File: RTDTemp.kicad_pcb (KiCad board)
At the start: 2 copper layers, 80 x 100 mm, 109 parts, among them J1 Conn_01x02, J2 Conn_01x02, J3 Car Power, J4 CAN_In, J5 CAN_Out, SW1 SW_Push, U1 Nucleo_L432KC, U2 PWR_REG_PQMC3-Dx-Sx-S, U3 ADM3055E, U4 CDSOT23-T24CAN

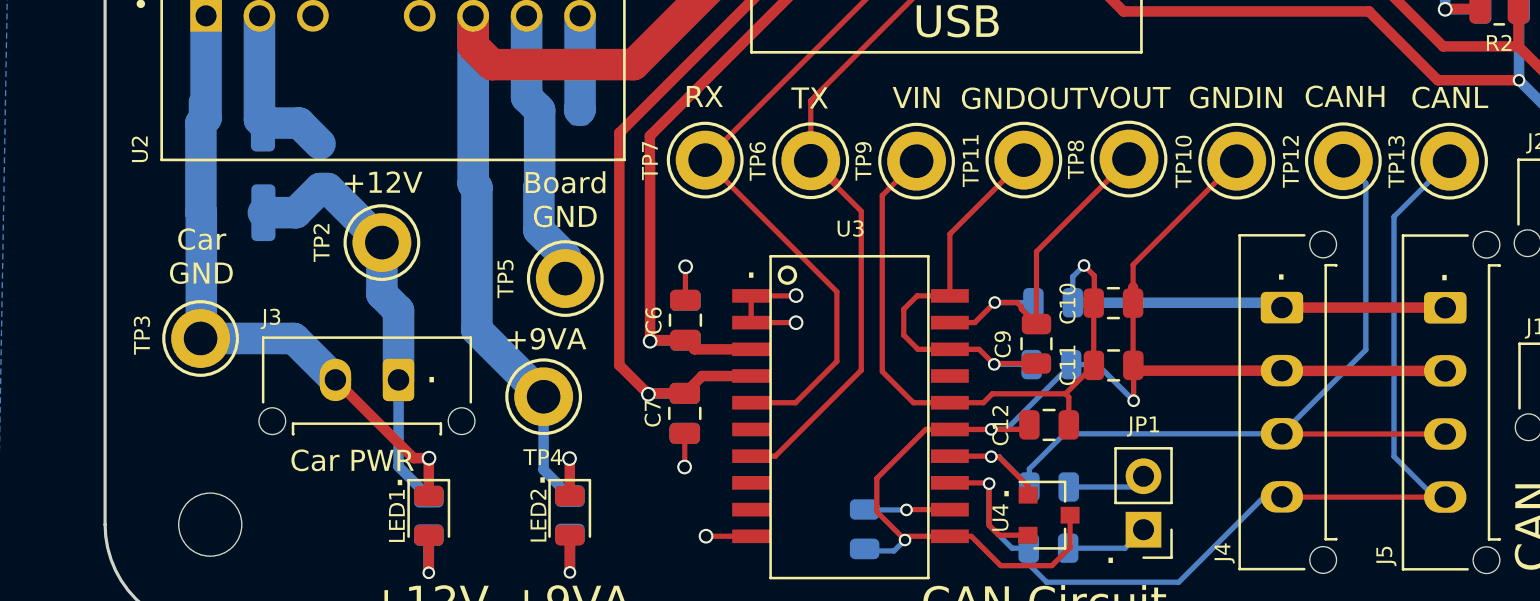
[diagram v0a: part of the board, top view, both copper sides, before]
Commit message: Updated README with assembly and testing instructions.
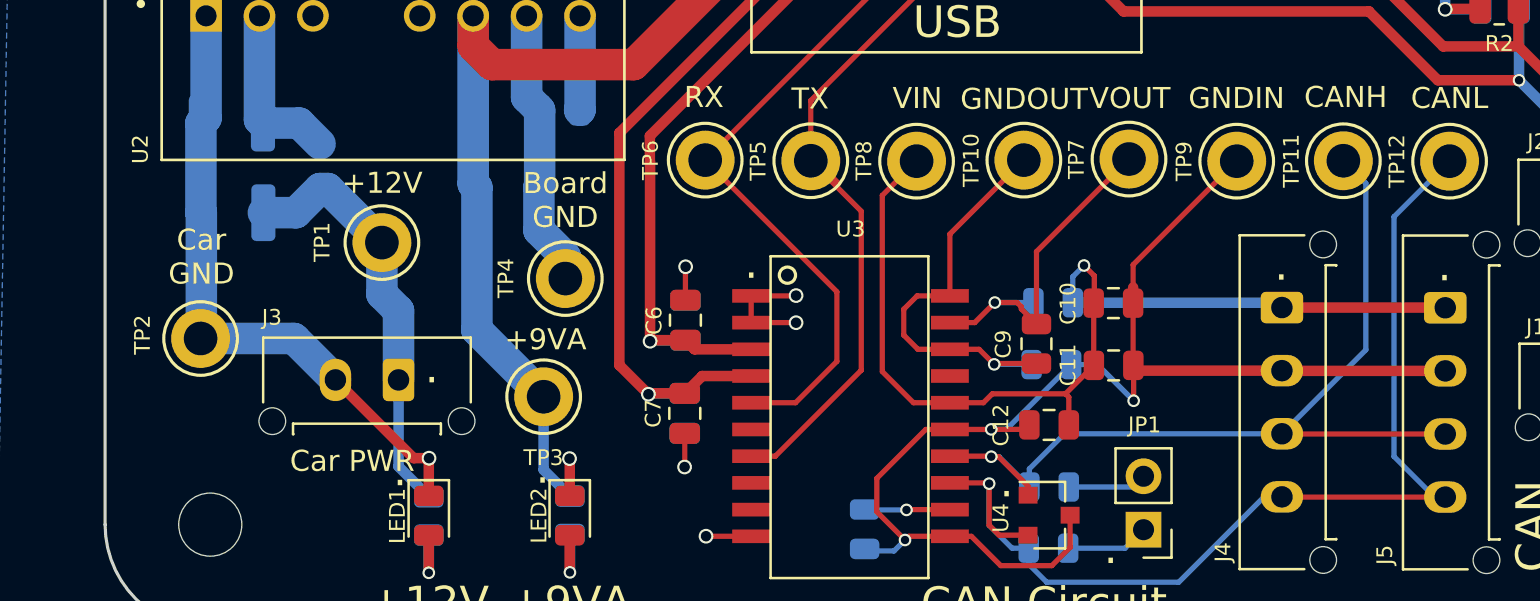
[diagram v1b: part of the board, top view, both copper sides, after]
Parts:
- renumbered TP2 to TP1, TP11 to TP10, TP12 to TP11, TP13 to TP12, TP3 to TP2, TP4 to TP3, TP5 to TP4, TP6 to TP5, TP7 to TP6, TP8 to TP7, TP9 to TP8, TP10 to TP9
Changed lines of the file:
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@@
   (general
     (thickness 1.6)
-    (drawings 224)
+    (drawings 223)
     (tracks 1386)
     (zones 0)
@@
   (page USLetter)
   (title_block
-    (title "UT SVT MPPT 2018")
-    (date 2018-10-31)
-    (rev Rev1.2+)
+    (title "Array RTD/Irradiance Sensor Board")
+    (date 2020-12-13)
+    (rev 1.0.0)
     (company "UT Solar Vehicle Team")
-    (comment 1 "See Schematic Rev3.1+.")
+    (comment 1 "Matthew Yu")
+    (comment 2 "Jacob Giddens")
+    (comment 3 "Gary Hallock")
   )
   (layers
@@
     (38 B.Mask user)
     (39 F.Mask user)
-    (40 Dwgs.User user hide)
-    (41 Cmts.User user hide)
+    (40 Dwgs.User user)
+    (41 Cmts.User user)
     (42 Eco1.User user)
     (43 Eco2.User user)
@@
     (descr "Keystone Miniature THM Test Point 5005-5009, http://www.keyelco.com/product-pdf.cfm?p=1314")
     (tags "Through Hole Mount Test Points")
-    (fp_text reference TP12 (at 0 -2.47 90) (layer F.SilkS)
+    (fp_text reference TP11 (at 0 -2.47 90) (layer F.SilkS)
       (effects (font (size 0.75 0.75) (thickness 0.15)))
     )
@@
     (descr "Keystone Miniature THM Test Point 5005-5009, http://www.keyelco.com/product-pdf.cfm?p=1314")
     (tags "Through Hole Mount Test Points")
-    (fp_text reference TP5 (at -2.82 -0.02 90) (layer F.SilkS)
+    (fp_text reference TP4 (at -2.82 -0.02 90) (layer F.SilkS)
       (effects (font (size 0.75 0.75) (thickness 0.15)))
     )
@@
     (descr "Keystone Miniature THM Test Point 5005-5009, http://www.keyelco.com/product-pdf.cfm?p=1314")
     (tags "Through Hole Mount Test Points")
-    (fp_text reference TP4 (at -0.01 2.9) (layer F.SilkS)
+    (fp_text reference TP3 (at -0.01 2.9) (layer F.SilkS)
       (effects (font (size 0.75 0.75) (thickness 0.15)))
     )
@@
     (descr "Keystone Miniature THM Test Point 5005-5009, http://www.keyelco.com/product-pdf.cfm?p=1314")
     (tags "Through Hole Mount Test Points")
-    (fp_text reference TP3 (at -2.76 -0.18 90) (layer F.SilkS)
+    (fp_text reference TP2 (at -2.76 -0.18 90) (layer F.SilkS)
       (effects (font (size 0.75 0.75) (thickness 0.15)))
     )
@@
     (descr "Keystone Miniature THM Test Point 5005-5009, http://www.keyelco.com/product-pdf.cfm?p=1314")
     (tags "Through Hole Mount Test Points")
-    (fp_text reference TP2 (at -2.84 -0.03 90) (layer F.SilkS)
+    (fp_text reference TP1 (at -2.84 -0.03 90) (layer F.SilkS)
       (effects (font (size 0.75 0.75) (thickness 0.15)))
     )
@@
     (descr "Keystone Miniature THM Test Point 5005-5009, http://www.keyelco.com/product-pdf.cfm?p=1314")
     (tags "Through Hole Mount Test Points")
-    (fp_text reference TP7 (at 0 -2.6 90) (layer F.SilkS)
+    (fp_text reference TP6 (at 0 -2.6 90) (layer F.SilkS)
       (effects (font (size 0.75 0.75) (thickness 0.15)))
     )
@@
     (descr "Keystone Miniature THM Test Point 5005-5009, http://www.keyelco.com/product-pdf.cfm?p=1314")
     (tags "Through Hole Mount Test Points")
-    (fp_text reference TP6 (at 0 -2.5 90) (layer F.SilkS)
+    (fp_text reference TP5 (at 0 -2.5 90) (layer F.SilkS)
       (effects (font (size 0.75 0.75) (thickness 0.15)))
     )
@@
     (descr "Keystone Miniature THM Test Point 5005-5009, http://www.keyelco.com/product-pdf.cfm?p=1314")
     (tags "Through Hole Mount Test Points")
-    (fp_text reference TP11 (at -2.5 0 270) (layer F.SilkS)
+    (fp_text reference TP10 (at -2.5 0 270) (layer F.SilkS)
       (effects (font (size 0.75 0.75) (thickness 0.15)))
     )
@@
     (descr "Keystone Miniature THM Test Point 5005-5009, http://www.keyelco.com/product-pdf.cfm?p=1314")
     (tags "Through Hole Mount Test Points")
-    (fp_text reference TP13 (at 0 -2.5 90) (layer F.SilkS)
+    (fp_text reference TP12 (at 0 -2.5 90) (layer F.SilkS)
       (effects (font (size 0.75 0.75) (thickness 0.15)))
     )
@@
     (descr "Keystone Miniature THM Test Point 5005-5009, http://www.keyelco.com/product-pdf.cfm?p=1314")
     (tags "Through Hole Mount Test Points")
-    (fp_text reference TP10 (at 0 2.5 90) (layer F.SilkS)
+    (fp_text reference TP9 (at 0 2.5 90) (layer F.SilkS)
       (effects (font (size 0.75 0.75) (thickness 0.15)))
     )
@@
     (descr "Keystone Miniature THM Test Point 5005-5009, http://www.keyelco.com/product-pdf.cfm?p=1314")
     (tags "Through Hole Mount Test Points")
-    (fp_text reference TP9 (at -0.03 2.5 90) (layer F.SilkS)
+    (fp_text reference TP8 (at -0.03 2.5 90) (layer F.SilkS)
       (effects (font (size 0.75 0.75) (thickness 0.15)))
     )
@@
     (descr "Keystone Miniature THM Test Point 5005-5009, http://www.keyelco.com/product-pdf.cfm?p=1314")
     (tags "Through Hole Mount Test Points")
-    (fp_text reference TP8 (at -2.5 0 270) (layer F.SilkS)
+    (fp_text reference TP7 (at -2.5 0 270) (layer F.SilkS)
       (effects (font (size 0.75 0.75) (thickness 0.15)))
     )
@@
     (effects (font (size 1 0.98) (thickness 0.15)) (justify mirror))
   )
-  (dimension 5 (width 0.15) (layer Dwgs.User)
-    (gr_text "5.000 mm" (at -121.27 21.24 90) (layer Dwgs.User)
-      (effects (font (size 1 1) (thickness 0.15)))
-    )
-    (feature1 (pts (xy -123.18 18.74) (xy -121.983579 18.74)))
-    (feature2 (pts (xy -123.18 23.74) (xy -121.983579 23.74)))
-    (crossbar (pts (xy -122.57 23.74) (xy -122.57 18.74)))
-    (arrow1a (pts (xy -122.57 18.74) (xy -121.983579 19.866504)))
-    (arrow1b (pts (xy -122.57 18.74) (xy -123.156421 19.866504)))
-    (arrow2a (pts (xy -122.57 23.74) (xy -121.983579 22.613496)))
-    (arrow2b (pts (xy -122.57 23.74) (xy -123.156421 22.613496)))
-  )
   (dimension 80.000002 (width 0.15) (layer Dwgs.User)

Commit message: Added zip and step files
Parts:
- moved J2 0.76 mm to (94.4, 99.7)
- moved J1 0.76 mm to (94.4, 108.4)
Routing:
- net Net-(J1-Pad1): track 64.1 -> 65.5 mm
